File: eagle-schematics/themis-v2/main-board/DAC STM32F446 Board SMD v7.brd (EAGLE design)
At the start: 163.3 x 142.1 mm, 250 parts, among them IC1 4027D, U2 AD5328BRUZ-REEL7, U3 AD5328BRUZ-REEL7

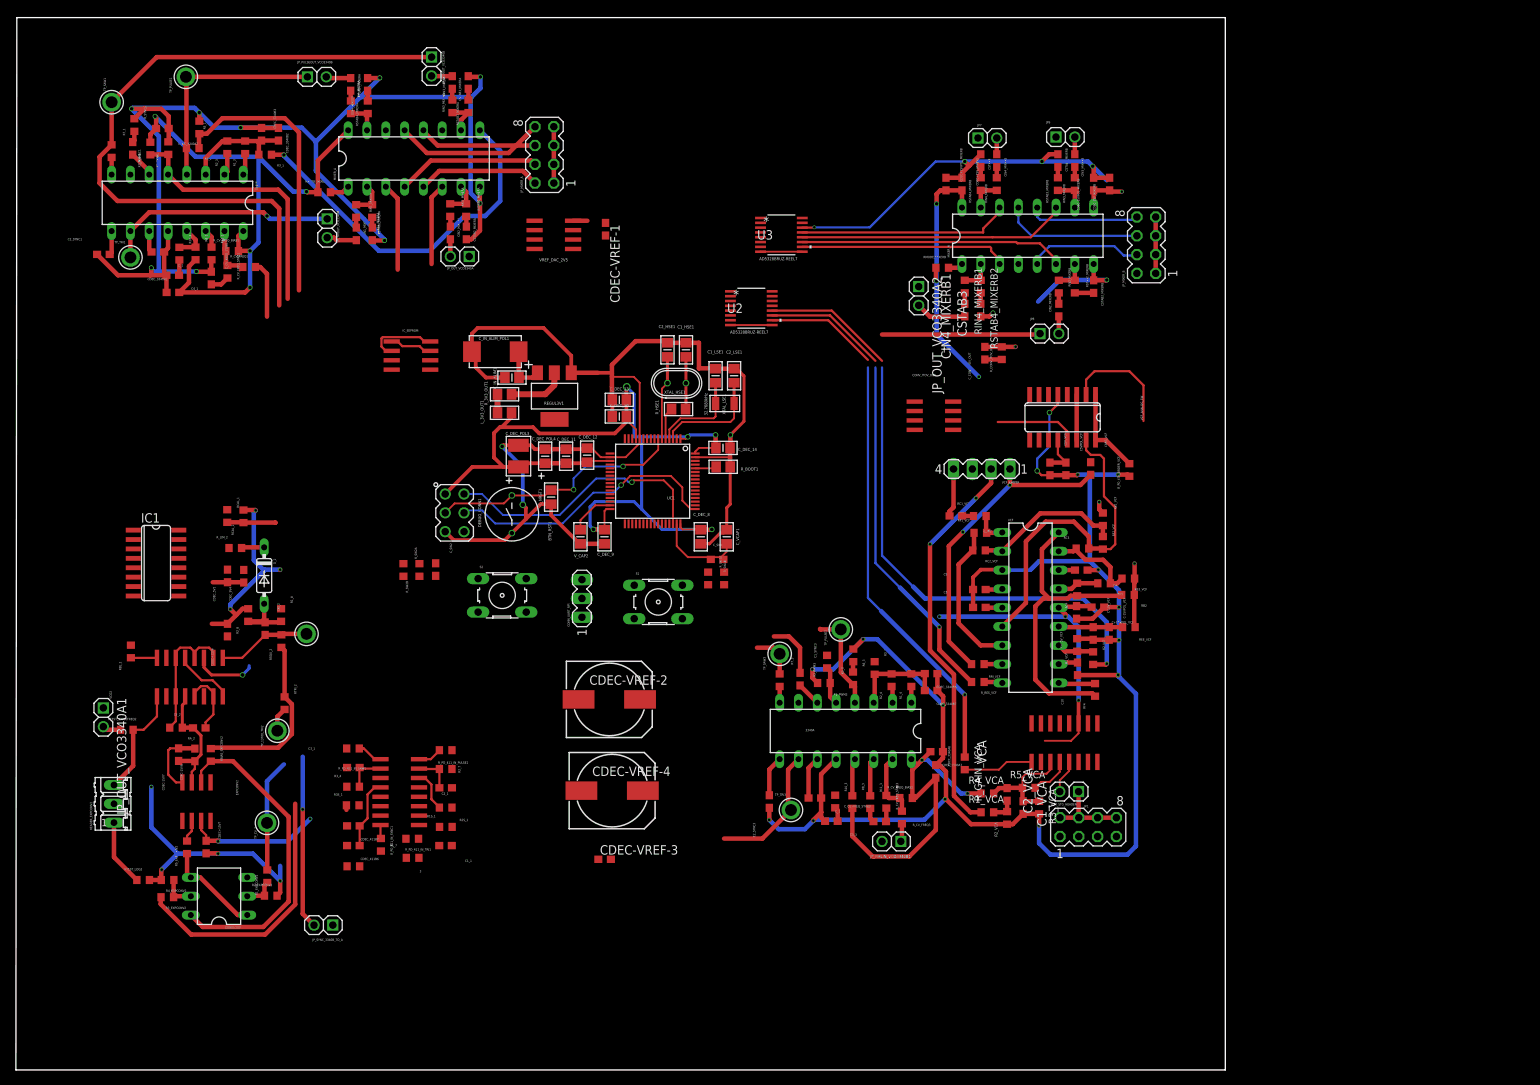
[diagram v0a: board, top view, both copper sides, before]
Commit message: started PCB routing with F446
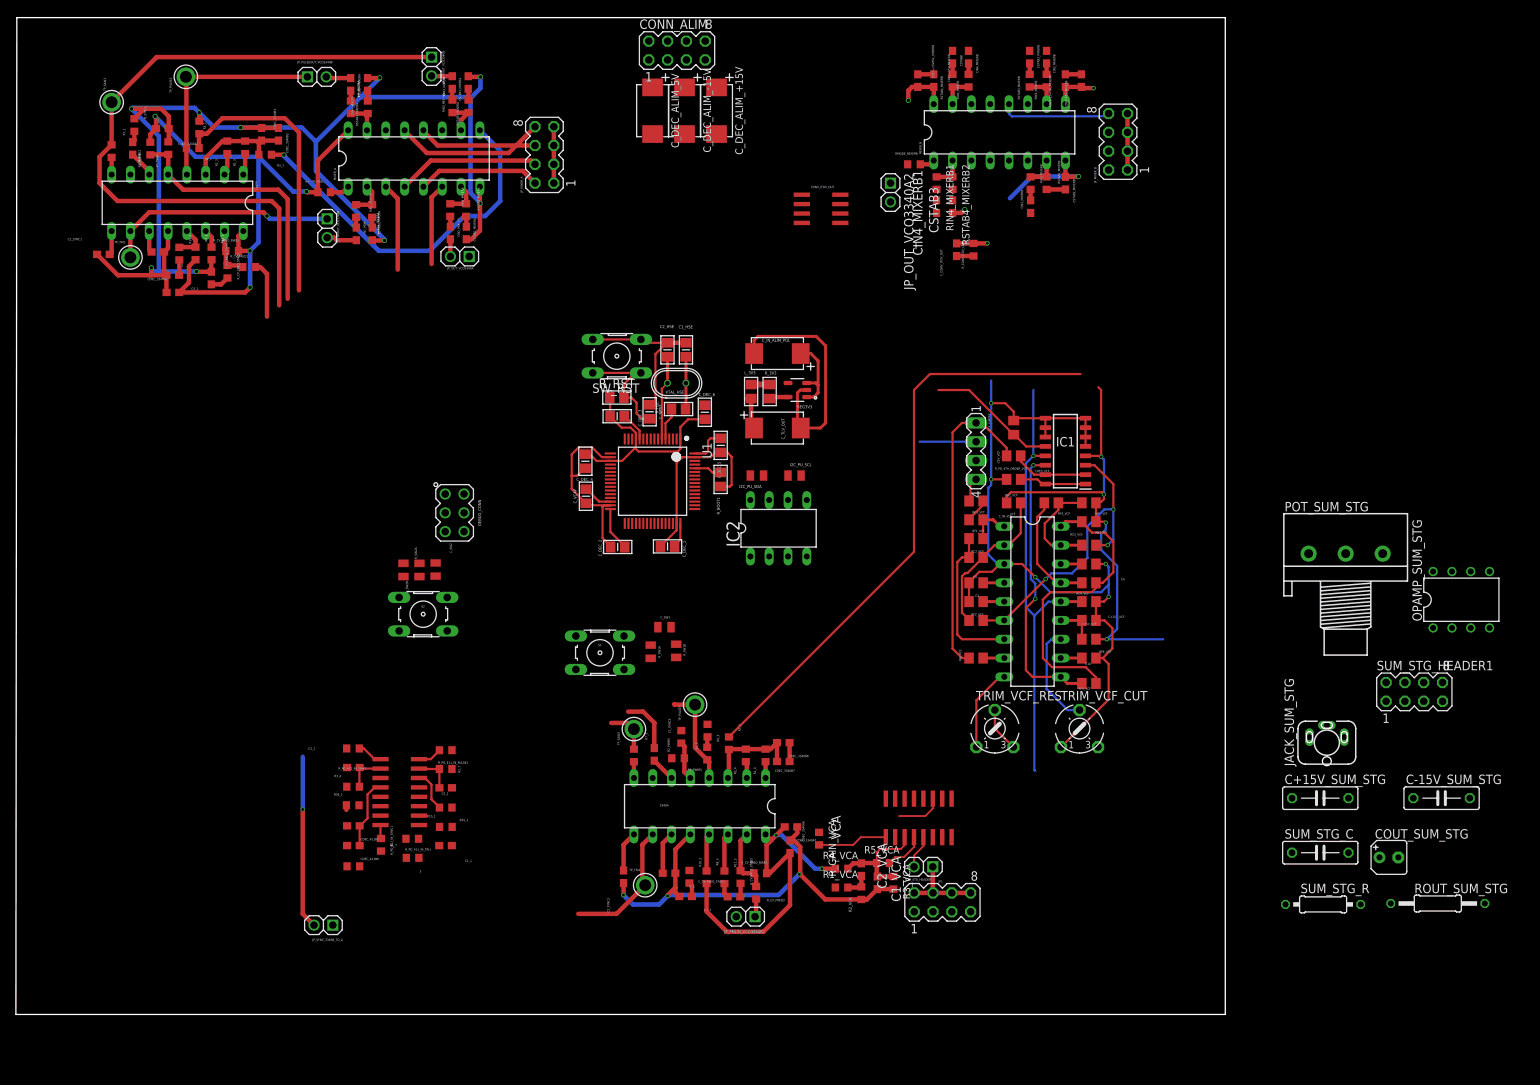
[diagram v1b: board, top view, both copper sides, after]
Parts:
- removed BTN_RST1: BUTTON-FSM14JRT, MyComponents:BUTTON-FSM14JRT
- removed C+15VPOL_VCF, C-15VPOL_VCF: 1u, rcl:C0603
- removed C1_LSE1, C2_LSE1: 22pF, MyComponents:C0805
- removed C5VPOL_VCF, CDEC+15V6, CDEC+15V7, CDEC-15V6, CDEC-15V7, CDEC-VREF-1, CDEC-VREF-3, CDEC_5V4: 100n, rcl:C0603
- removed CDEC-VREF-2: 10u, rcl:140CLH-1014
- removed CDEC-VREF-4: 100u, rcl:140CLH-1014
- removed CDEC_5V1: 10u, rcl:C0603
- removed CF_2: 100nF, rcl:C0603
- removed CIN_2, C_IN2: 470n, rcl:C0603
- removed CONN_UART_RPI: (no value), con-lstb:MA03-1
- removed CONVLOG2: BC857BS, paires_diff:DIL06
- removed C_DEC_10, C_DEC_12, C_DEC_14, C_DEC_8, C_DEC_9, C_IN_ALIM1, C_NRST1: 0.1uF, MyComponents:C0805
- removed C_DEC_11: 4.7uF, MyComponents:C0805
- removed C_DEC_13: 1.0uF, MyComponents:C0805
- removed C_DEC_POL3: 100 uF, MyComponents:CPOL1311
- removed C_DEC_POL4: 47 uF, MyComponents:CPOL0805
- removed C_IN_ALIM_POL1: 470 uF, MyComponents:CPOL2917
- removed C_VCAP1, V_CAP2: 2.2uF, MyComponents:C0805
- removed D_2: 1N4148DO35-7, diode:DO35-7
- removed EXPCONV2: TL081, linear:SO08
- removed HEADER_EXPCONV2: (no value), con-amp-quick:03P
- removed IC_EEPROM: 24C04ASN, microchip:SO-08
- removed JP7, JP8, JP9, JP_OUT_VCO3340A1: JUMPER, 6P1_EVB:HDR2X1
- removed L_3V3_OUT1: 1 uH, MyComponents:L0805
- removed R1_8, R2_8, R2_VCF, RCAL_2, RF3, RF4, R_RES_VCF: 100k, rcl:R0603
- removed R1_EXPCONV2: 330, rcl:R0603
- removed R1_VCF, RSQU_2: 10k, rcl:R0603
- removed R2_EXPCONV2, R4_EXPCONV2: 10, rcl:R0603
- removed R3_EXPCONV2: 260, rcl:R0603
- removed R5_EXPCONV2: 110, rcl:R0603
- removed RA_2: 4.7k, rcl:R0603
- removed RB2: 220k, rcl:R0603
- removed RBIAS_EXPCONV2, RCAL_1: 47k, rcl:R0603
- removed RC3, RC4: 91k, rcl:R0603
- removed REE_2, RTEST_13700FREQ2: 27k, rcl:R0603
- removed REGUL3V1: REG1117, MyComponents:SOT223
- removed RTEST_LOG2, R_LIM_2: 1k, rcl:R0603
- removed RTRI_2: 12k, rcl:R0603
- removed R_3V3_OUT1: 1, MyComponents:R0805
- removed TP_13700_SQU2, TP_13700_TRI2, TP_CV_2: (no value), 6P1_EVB:TESTPOINT_63
- removed U2, U3: AD5328BRUZ-REEL7, AD5328:RU_16
- removed UC1: STM32F405RG, stm32:LQFP64
- removed VCF_ANALOG_SW: DG413DJD, linear:SO16
- removed VCO2: LM13700M, ota:SO16
- removed VREF_DAC_2V5: AD780R, analog-devices:SO8
- removed XTAL_LSE1: 32.7680kHz, MyComponents:Q-CM7V-T1A
- added C+15V_SUM_STG, C-15V_SUM_STG: 100n, rcl:C075-032X103
- added CONN_ALIM, SUM_STG_HEADER1: (no value), con-lstb:MA04-2
- added COUT_SUM_STG: 22u, resistor:B45181A
- added C_DEC_1, C_DEC_2, C_DEC_3, C_DEC_4, C_DEC_5, C_NRST: 0.1uF, MyComponents:C0805
- added C_DEC_6: 1.0uF, MyComponents:C0805
- added C_DEC_ALIM_+15V, C_DEC_ALIM_-15V, C_DEC_ALIM_5V, C_IN_ALIM_POL: 10u, MyComponents:CPOL2917
- added C_IN_VCF: 470n, rcl:C0805
- added C_TLV_OUT: 100 uF, MyComponents:CPOL2917
- added C_VCAP: 2.2uF, MyComponents:C0805
- added I2C_PU_SCL, I2C_PU_SDA: 1k, 6P1_EVB:R0805
- added IC2: 24C04AP, microchip:DIL8
- added JACK_SUM_STG: 1502_01, con-lumberg:1502_01
- added L_3V3: 1 uH, MyComponents:L0805
- added OPAMP_SUM_STG: NE5534AN, linear:DIL08
- added POT_SUM_STG: 100kB, pot:3RP/1610N
- added RB2_VCF: 220k, rcl:R0805
- added RC3_VCF, RC4_VCF: 91k, rcl:R0805
- added REG3V3: TLV75533PDBVR, TLV75533PDBVR:SOT95P280X145-5N
- added RF3_VCF, RF4_VCF: 100k, rcl:R0805
- added ROUT_SUM_STG: 470, rcl:0207/12
- added R_3V3: 1, MyComponents:R0805
- added R_RST: 100k, MyComponents:R0805
- added SUM_STG_C: 560p, rcl:C075-032X103
- added SUM_STG_R: 27k, rcl:0207/10
- added SW_RST: (no value), switch-omron:B3F-10XX
- added TRIM_VCF_CUT, TRIM_VCF_RES: 100k, adafruit:6MM
- added U1: STM32F446RCT7, STM32F446RCT7:QFP50P1200X1200X160-64N
- C+15V_VCF, C-15V_VCF, C10, C3, C4, C5, C5V_VCF, CRES_VCF: device rcl:C0603 -> rcl:C0805
- C_SW1, C_SW2: device 6P1_EVB:C0603 -> 6P1_EVB:C0805
- IC1: value 4027D -> ADG453BRZ; device 40xx:SO16 -> ADG453BRZ:SOIC127P600X175-16N
- RB1_VCF, RB3_VCF, RC1_VCF, RC2_VCF, REE_VCF, RF1_VCF, RF2_VCF, RRI_VCF, R_PD_4TH_ORDER_VCF: device rcl:R0603 -> rcl:R0805
- R_SW1A, R_SW1B, R_SW2A, R_SW2B: device 6P1_EVB:R0603 -> 6P1_EVB:R0805
- moved IC1 123.7 mm to (141.6, 76.2), turned to 180 degrees
- moved CONV_ITOV_OUT 31.8 mm to (108.6, 108.9)
- moved JP1 22.2 mm to (123.7, 20.1)
- moved R1_4 22.2 mm to (101.1, 35.1)
- moved R1_PWM3 22.2 mm to (89.3, 34.7)
- moved R2_4 22.2 mm to (98.4, 35.1)
- moved R7_3 22.2 mm to (83.3, 35.1)
- moved 3340A 22.2 mm to (92.2, 28.2)
- moved C2_SYNC3 22.2 mm to (81.9, 18.7)
- moved C4_3 22.2 mm to (90.3, 16.1)
- moved CDEC_3340A6 22.2 mm to (104.4, 22.8)
- moved CDEC_3340A7 22.2 mm to (104.5, 25.5)
- moved C_3 22.2 mm to (88.1, 19.2)
- moved C_CV_FREQ_STAB3 22.2 mm to (96.8, 16.0)
- moved JP_FMLIN_VCO3340B1 22.2 mm to (99.7, 13.3)
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- renumbered C1_HSE1 to C1_HSE, C2_HSE1 to C2_HSE, DEBUG_CONN1 to DEBUG_CONN, R_HSE1 to R_HSE, XTAL_HSE1 to XTAL_HSE
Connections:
- removed net ALIM_CONN: C_IN_ALIM1.1, C_IN_ALIM_POL1.+, REGUL3V1.3
- removed net BIAS_4027_VCO13700: CIN_2.1, D_2.A, R1_8.2, R2_8.1
- removed net CALIB_13700: RCAL_1.2, RCAL_2.1
- removed net CV_FREQ_13700: R1_EXPCONV2.2, TP_CV_2.P$1, U2.6
- removed net DAC_LDAC: U2.1, U3.1
- removed net DAC_SYNC_CV: U2.2
- removed net DAC_SYNC_GAIN: U3.2
- removed net FM_ENTREE_13700_VCO13700: HEADER_EXPCONV2.3, RTEST_13700FREQ2.2, VCO2.1
- removed net IA_VCO13700: REE_2.1, VCO2.16
- removed net INPUT_FM_3340: JP_OUT_VCO3340A1.2, RTEST_13700FREQ2.1
- removed net N$105: C2_HSE.2, UC1.6, XTAL_HSE.2
- removed net N$106: R_HSE.1, UC1.5
- removed net N$113: CRES_VCF.1, VCF_ANALOG_SW.14, VCF_ANALOG_SW.3
- removed net N$94: EXPCONV2.6, R5_EXPCONV2.2
- removed net N$95: RA_2.2, VCO2.10, VCO2.12, VCO2.14, VCO2.3
- removed net N$96: CF_2.2, VCO2.5, VCO2.7
- removed net N$98: D_2.C, R_LIM_2.2
- removed net N$99: HEADER_EXPCONV2.1, RTEST_LOG2.1
- removed net OUT_EXPCONV_VCO13700: CONVLOG2.3, HEADER_EXPCONV2.2
- removed net PA0: UC1.14
- removed net PA1: UC1.15
- removed net PA10: UC1.43
- removed net PA15: UC1.50
- removed net PA2: UC1.16
- removed net PA3: UC1.17
- removed net PA4: UC1.20
- removed net PA5: UC1.21
- removed net PA6: UC1.22
- removed net PA7: UC1.23
- removed net PA8: UC1.41
- removed net PB0: UC1.26
- removed net PB1: UC1.27
- removed net PB10: UC1.29
- removed net PB11: UC1.30
- removed net PB12: UC1.33
- removed net PB13: UC1.34
- removed net PB14: UC1.35
- removed net PB15: UC1.36
- removed net PB2: UC1.28
- removed net PB3: UC1.55
- removed net PB4: UC1.56
- removed net PB5: UC1.57
- removed net PB6: UC1.58
- removed net PB7: UC1.59
- removed net PB8: UC1.61
- removed net PB9: UC1.62
- removed net PC0: UC1.8
- removed net PC1: UC1.9
- removed net PC10: UC1.51
- removed net PC11: UC1.52
- removed net PC12: UC1.53
- removed net PC13: UC1.2
- removed net PC2: UC1.10
- removed net PC3: UC1.11
- removed net PC4: UC1.24
- removed net PC5: UC1.25
- removed net PC6: UC1.37
- removed net PC7: UC1.38
- removed net PC8: UC1.39
- removed net PC9: UC1.40
- removed net PD2: UC1.54
- removed net PNP1_B_VCO13700: CONVLOG2.2, R1_EXPCONV2.1, R2_EXPCONV2.1
- removed net PNP1_C1_VCO1: CONVLOG2.6, EXPCONV2.2, RBIAS_EXPCONV2.2
- removed net PNP2_B_VCO13700: CONVLOG2.5, R3_EXPCONV2.1, R4_EXPCONV2.1
- removed net PNP_E1-VCO1_MIXB: CONVLOG2.1, CONVLOG2.4, R5_EXPCONV2.1
- removed net Q2M1: C2_LSE1.2, UC1.3, XTAL_LSE1.1
- removed net Q2P1: C1_LSE1.2, UC1.4, XTAL_LSE1.2
- removed net SPI_CLK: U2.16, U3.16
- removed net SPI_MOSI: U2.15, U3.15
- removed net SUBBASS_IN_VCO13700: IC1.13, R_LIM_2.1
- removed net USART_RX_RPI_TX: CONN_UART_RPI.2
- removed net USART_TX_RPI_RX: CONN_UART_RPI.3
- removed net USB-DM: UC1.44
- removed net USB-DP: UC1.45
- removed net USB-VBUS: UC1.42
- removed net VCAP2: UC1.31, V_CAP2.2
- removed net VCO13700_SQUARE: CIN_2.2, JP8.1, RSQU_2.2, TP_13700_SQU2.P$1, VCO2.9
- removed net VCO13700_SUBBASS: IC1.15, JP7.1, RCAL_1.1
- removed net VCO13700_TRI: JP9.1, RTRI_2.2, TP_13700_TRI2.P$1, VCO2.13, VCO2.8
- removed net VDD: C_DEC_10.2, C_DEC_11.2, C_DEC_12.2, C_DEC_13.2, C_DEC_14.2, C_DEC_8.2, C_DEC_9.2, C_DEC_POL3.1+, C_DEC_POL4.1+, DEBUG_CONN.1, L_3V3_OUT1.2, UC1.1, UC1.13, UC1.19, UC1.32, UC1.48, UC1.64
- removed net VREF: CDEC-VREF-4.+, U2.8, U2.9, U3.8, U3.9, VREF_DAC_2V5.6
- new net 3V3: C_DEC_1.2, C_DEC_2.2, C_DEC_3.2, C_DEC_4.2, C_DEC_5.2, C_DEC_6.2, C_TLV_OUT.+, DEBUG_CONN.1, I2C_PU_SCL.2, I2C_PU_SDA.2, IC2.2, IC2.3, IC2.8, L_3V3.2, R_RST.1, R_SW1A.1, R_SW2A.1, U1.1, U1.13, U1.19, U1.32, U1.48, U1.64
- new net CALIB_3340C: U1.16
- new net FEEDBACK_VCF: CRES_VCF.1, IC1.15, IC1.2
- new net JACK_SUM_STG: COUT_SUM_STG.-, JACK_SUM_STG.3
- new net OSC_IN: R_HSE.1, U1.5
- new net OSC_OUT: C2_HSE.2, U1.6, XTAL_HSE.2
- new net OUT_SUM_STG: OPAMP_SUM_STG.6, ROUT_SUM_STG.2, SUM_STG_C.1, SUM_STG_R.1
- new net POT2_SUM_STG: COUT_SUM_STG.+, POT_SUM_STG.2
- new net POT3_SUM_STG: POT_SUM_STG.3, ROUT_SUM_STG.1
- net +15V: now also C+15V_SUM_STG.2, CONN_ALIM.7, CONN_ALIM.8, C_DEC_ALIM_+15V.+, IC1.13, OPAMP_SUM_STG.7; no longer C+15VPOL_VCF.2, CDEC+15V6.1, CDEC+15V7.1, EXPCONV2.7, VCF_ANALOG_SW.13, VCO2.11
- net -15V: now also C-15V_SUM_STG.1, CONN_ALIM.5, CONN_ALIM.6, C_DEC_ALIM_-15V.+, IC1.4, OPAMP_SUM_STG.4, RB2_VCF.1; no longer CDEC-15V6.2, CDEC-15V7.2, EXPCONV2.4, RB2.1, RBIAS_EXPCONV2.1, RSQU_2.1, RTRI_2.1, VCF_ANALOG_SW.4, VCO2.6
- net 411_IN_PULSE: now also U1.40
- net 411_IN_SAW: now also U1.38
- net 411_IN_SYNC: now also U1.37
- net 411_IN_TRI: now also U1.39
- net 5V: now also CONN_ALIM.3, CONN_ALIM.4, C_DEC_ALIM_5V.+, C_IN_ALIM_POL.+, IC1.12, REG3V3.1, REG3V3.3; no longer C5VPOL_VCF.1, CDEC-VREF-1.2, CDEC-VREF-2.-, CDEC_5V1.1, CDEC_5V4.1, IC1.11, IC1.16, IC_EEPROM.2, IC_EEPROM.3, IC_EEPROM.8, R1_8.1, R3_EXPCONV2.2, R_SW1A.1, R_SW2A.1, U2.3, U3.3, VCF_ANALOG_SW.12, VREF_DAC_2V5.2
- net AGND: now also C+15V_SUM_STG.1, C-15V_SUM_STG.2, JACK_SUM_STG.1, OPAMP_SUM_STG.3, POT_SUM_STG.1; no longer C+15VPOL_VCF.1, C+15V_VCF.1, C-15VPOL_VCF.2, C-15V_VCF.2, C10.1, C3.1, C4.1, C5.1, C5VPOL_VCF.2, C5V_VCF.2, CDEC+15V6.2, CDEC+15V7.2, CDEC-15V6.1, CDEC-15V7.1, CDEC-VREF-1.1, CDEC-VREF-2.+, CDEC-VREF-3.2, CDEC-VREF-4.-, CDEC_5V1.2, CDEC_5V4.2, CF_2.1, CONN_UART_RPI.1, EXPCONV2.3, IC1.12, IC1.3, IC1.4, IC1.5, IC1.6, IC1.7, IC1.8, IC1.9, IC_EEPROM.1, IC_EEPROM.4, IC_EEPROM.7, R1_VCF.2, R2_8.2, R2_EXPCONV2.2, R4_EXPCONV2.2, RA_2.1, RCAL_2.2, REE_2.2, RTEST_LOG2.2, R_PD_4TH_ORDER_VCF.1, U2.14, U3.14, VCF.3, VCF_ANALOG_SW.5, VCO2.4, VREF_DAC_2V5.4, VREF_DAC_2V5.5
- net BOOT1: now also U1.60; no longer UC1.60
- net CALIB_3340A: now also U1.14
- net CALIB_3340B: now also U1.15
- net CV_CUTOFF: now also TRIM_VCF_CUT.E; no longer R2_VCF.2, U2.12
- net CV_FREQ_3340A: no longer U2.7
- net CV_FREQ_3340B: no longer U2.4
- net CV_PWM_3340A: no longer U2.13
- net CV_PWM_3340B: no longer U2.5
- net CV_RES: now also TRIM_VCF_RES.E, TRIM_VCF_RES.S; no longer R_RES_VCF.2, U2.11
- net CV_VCA: no longer U2.10
- net FREQ_CV_VCF: now also TRIM_VCF_CUT.S; no longer R1_VCF.1, R2_VCF.1
- net GAIN1_A: no longer U3.4
- net GAIN1_B: no longer U3.10
- net GAIN2_A: no longer U3.5
- net GAIN2_B: no longer U3.11
- net GAIN3_A: no longer U3.6
- net GAIN3_B: no longer U3.12
- net GAIN4_A: no longer U3.7
- net GAIN4_B: no longer U3.13
- net GND: now also C+15V_VCF.1, C-15V_VCF.2, C10.1, C3.1, C4.1, C5.1, C5V_VCF.2, CONN_ALIM.1, CONN_ALIM.2, C_DEC_1.1, C_DEC_2.1, C_DEC_3.1, C_DEC_4.1, C_DEC_5.1, C_DEC_6.1, C_DEC_ALIM_+15V.-, C_DEC_ALIM_-15V.-, C_DEC_ALIM_5V.-, C_IN_ALIM_POL.-, C_NRST.1, C_TLV_OUT.-, C_VCAP.1, IC1.10, IC1.11, IC1.5, IC1.6, IC1.7, IC1.8, IC1.9, IC2.1, IC2.4, IC2.7, REG3V3.2, R_PD_4TH_ORDER_VCF.1, SW_RST.3, SW_RST.4, TRIM_VCF_CUT.A, U1.12, U1.18, U1.31, U1.47, U1.63, VCF.3; no longer BTN_RST1.P$1, C1_LSE1.1, C2_LSE1.1, C_DEC_10.1, C_DEC_11.1, C_DEC_12.1, C_DEC_13.1, C_DEC_14.1, C_DEC_8.1, C_DEC_9.1, C_DEC_POL3.2-, C_DEC_POL4.2-, C_IN_ALIM1.2, C_IN_ALIM_POL1.-, C_NRST1.1, C_VCAP1.1, REGUL3V1.1, UC1.12, UC1.18, UC1.63, V_CAP2.1
- net IN2_MIXERA: no longer JP_OUT_VCO3340A2.1
- net IN2_MIXERB: no longer JP8.2
- net IN3_MIXERB: no longer JP9.2
- net IN3_VCF: now also RB2_VCF.2, RC3_VCF.1, RF3_VCF.1; no longer RB3_VCF.2, RC3.1, RF3.1
- net IN4_MIXERB: no longer JP7.2
- net IN4_VCF: now also RB3_VCF.2, RC4_VCF.1, RF4_VCF.1; no longer RB2.2, RC4.1, RF4.1
- net INPUT_CURRENT_SUM_STG: now also OPAMP_SUM_STG.2, SUM_STG_C.2, SUM_STG_HEADER1.1, SUM_STG_HEADER1.2, SUM_STG_HEADER1.3, SUM_STG_HEADER1.4, SUM_STG_HEADER1.5, SUM_STG_HEADER1.6, SUM_STG_HEADER1.7, SUM_STG_HEADER1.8, SUM_STG_R.2
- net IN_VCF: now also C_IN_VCF.2; no longer C_IN2.2
- net IN_VCFORDER: now also IC1.1, IC1.16; no longer VCF_ANALOG_SW.1, VCF_ANALOG_SW.16
- net N$1: now also JP_MIXER_B.2, MIXER_B.4; no longer JP_OUT_VCO3340A1.1
- net N$108: now also REG3V3.5, R_3V3.2; no longer REGUL3V1.2, R_3V3_OUT1.2
- net N$109: now also L_3V3.1, R_3V3.1; no longer L_3V3_OUT1.1, R_3V3_OUT1.1
- net N$116: now also C_IN_VCF.1; no longer C_IN2.1
- net N$3: now also JP_OUT_VCO3340A2.1; no longer CDEC-VREF-3.1, VREF_DAC_2V5.3
- net N$6: now also U1.10, U1.20, U1.21, U1.23, U1.29, U1.33, U1.34, U1.35, U1.36, U1.50, U1.51, U1.58, U1.59, U1.9; no longer IC1.10, IC1.14
- net NRST: now also C_NRST.2, R_RST.2, SW_RST.1, SW_RST.2, U1.7; no longer BTN_RST1.P$2, C_NRST1.2, UC1.7
- net OUT2_VCF: now also IC1.3, RC3_VCF.2; no longer RC3.2, VCF_ANALOG_SW.15
- net OUT3_VCF: now also RC4_VCF.2, RF3_VCF.2; no longer RC4.2, RF3.2
- net OUT4_VCF: now also IC1.14, RF4_VCF.2; no longer RF4.2, VCF_ANALOG_SW.2
- net RES_CUR_VCF: now also TRIM_VCF_RES.A; no longer R_RES_VCF.1
- net SCL: now also I2C_PU_SCL.1, IC2.6, U1.61; no longer IC_EEPROM.6
- net SDA: now also I2C_PU_SDA.1, IC2.5, U1.62; no longer IC_EEPROM.5
- net SWCLK: now also U1.49; no longer UC1.49
- net SWDIO: now also U1.46; no longer UC1.46
- net VCAP1: now also C_VCAP.2, U1.30; no longer C_VCAP1.2, UC1.47
- net VEE_VCF: no longer C-15VPOL_VCF.1
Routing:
- net AGND: track 574.3 -> 259.9 mm, vias 37 -> 14
- net VDD: track 126.3 -> 0.00 mm, vias 5 -> 0
- net -15V: track 99.3 -> 200.4 mm, vias 4 -> 6
- net CV_CUTOFF: track 84.6 -> 0.00 mm, vias 1 -> 0
- net CV_VCA: track 73.2 -> 0.00 mm, vias 1 -> 0
- net CV_RES: track 64.3 -> 6.04 mm, vias 1 -> 0
- net GND: track 164.8 -> 219.1 mm, vias 3 -> 5
- net 3V3: track 0.00 -> 49.3 mm
- net IN_VCA: track 53.5 -> 7.62 mm, vias 2 -> 0
- net PNP1_C1_VCO1: track 43.8 -> 0.00 mm
- net +15V: track 242.7 -> 200.4 mm, vias 15 -> 8
- net SWCLK: track 37.7 -> 0.00 mm, vias 1 -> 0
- net SWDIO: track 36.9 -> 0.00 mm, vias 1 -> 0
- net GAIN3_B: track 36.3 -> 0.00 mm
- net GAIN2_B: track 35.8 -> 0.00 mm
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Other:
- board size 163.3 x 142.1 mm -> 163.3 x 134.6 mm

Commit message: PCB for F446
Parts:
- removed 3: ADG411R, analog-devices:SOIC16N
- removed C+15V_SUM_STG, C-15V_SUM_STG: 100n, rcl:C075-032X103
- removed C+15V_VCF, C-15V_VCF, C5V_VCF: 100n, rcl:C0805
- removed C1_1, C2_1, C3_1, CIN1_MIXERA, CIN2_MIXERA, CIN2_MIXERB, CIN3_MIXERA, CIN3_MIXERB, CIN4_MIXERA, CIN4_MIXERB, CIN4_MIXERB1: 470n, rcl:C0603
- removed C1_HSE, C2_HSE: 12pF, MyComponents:C0805
- removed C1_SYNC1, C1_SYNC3, C_1, C_3: 1n, rcl:C0603
- removed C1_VCA, C2_VCA: 4.7u, rcl:C0603
- removed C2_SYNC1, C2_SYNC3, CDEC+15VPOL_MIXERB, CDEC+15V_MIXERB, CDEC-15VPOL_MIXERB, CDEC-15V_MIXERB, CDEC_3340A2, CDEC_3340A6, CDEC_3340B2, CDEC_3340B6, CDEC_411B6: 100n, rcl:C0603
- removed C4_1, C4_3, C_CV_FREQ_STAB1, C_CV_FREQ_STAB3: 10n, rcl:C0603
- removed CDEC_3340A3, CDEC_3340A7, CDEC_3340B3, CDEC_3340B7, CDEC_411B7: 10u, rcl:C0603
- removed CONN_ALIM, JP_MIXER_A, JP_MIXER_B, SUM_STG_HEADER, SUM_STG_HEADER1: (no value), con-lstb:MA04-2
- removed CONV_ITOV_OUT: NE5534AD, linear:SO08
- removed COUT_SUM_STG: 22u, resistor:B45181A
- removed CRES_VCF: 1u, rcl:C0805
- removed CSTAB1_MIXERA, CSTAB2_MIXERA, CSTAB2_MIXERB, CSTAB3, CSTAB3_MIXERA, CSTAB3_MIXERB, CSTAB4_MIXERA, CSTAB8: 560p, rcl:C0603
- removed C_CONV_ITOV_OUT: 1p, rcl:C0603
- removed C_DEC_1, C_DEC_2, C_DEC_3, C_DEC_4, C_DEC_5, C_NRST: 0.1uF, MyComponents:C0805
- removed C_DEC_6: 1.0uF, MyComponents:C0805
- removed C_DEC_ALIM_+15V, C_DEC_ALIM_-15V, C_DEC_ALIM_5V, C_IN_ALIM_POL: 10u, MyComponents:CPOL2917
- removed C_IN_VCF: 470n, rcl:C0805
- removed C_SW1, C_SW2: 100n, 6P1_EVB:C0805
- removed C_TLV_OUT: 100 uF, MyComponents:CPOL2917
- removed C_VCAP: 2.2uF, MyComponents:C0805
- removed DEBUG_CONN: 75867-331LF, MyComponents:MA03-2
- removed I2C_PU_SCL, I2C_PU_SDA: 1k, 6P1_EVB:R0805
- removed IC1: ADG453BRZ, ADG453BRZ:SOIC127P600X175-16N
- removed IC2: 24C04AP, microchip:DIL8
- removed JACK_SUM_STG: 1502_01, con-lumberg:1502_01
- removed JP1, JP_FMLIN_VCO3340B1, JP_OUT_VCO3340A, JP_OUT_VCO3340A2, JP_PULSEOUT_VCO3340B, JP_SAWOUT_VCO3340B, JP_SYNC_3340B_TO_A, JP_TRIOUT_VCO3340B: JUMPER, 6P1_EVB:HDR2X1
- removed L_3V3: 1 uH, MyComponents:L0805
- removed MIXER_A, MIXER_B: SSM2164_MULTI, analog-audio-chips:DIL16
- removed OPAMP_SUM_STG: NE5534AN, linear:DIL08
- removed POT_SUM_STG: 100kB, pot:3RP/1610N
- removed R10_1, R10_3, RSTAB1_MIXERA, RSTAB2_MIXERA, RSTAB2_MIXERB, RSTAB3_MIXERA, RSTAB3_MIXERB, RSTAB4_MIXERA, RSTAB4_MIXERB, RSTAB4_MIXERB2, R_CV_FREQ_STAB1, R_CV_FREQ_STAB3: 470, rcl:R0603
- removed R11_1, R11_3: 1.8k, rcl:R0603
- removed R1S_1, R2S_1, R3S_1: 1k, rcl:R0603
- removed R1_3, R1_4: 30k, rcl:R0603
- removed R1_7, R2_7, R3_4, R5_VCA, R_PD_411_IN_PULSE1, R_PD_411_IN_SAW1, R_PD_411_IN_SYNC1, R_PD_411_IN_TRI1: 100k, rcl:R0603
- removed R1_PWM1, R1_PWM3, R_CV_FREQ1, R_CV_FREQ3: 68k, rcl:R0603
- removed R1_VCA, R2_VCA, R3_VCA, R4_VCA, R5_1, R5_3: 10k, rcl:R0603
- removed R2_3, R2_4, R7_1, R7_3: 5.6k, rcl:R0603
- removed R2_PWM1, R2_PWM3: 330k, rcl:R0603
- removed R3_1, R3_3: 820, rcl:R0603
- removed R6_1, R6_3: 33k, rcl:R0603
- removed R8_1, R8_3: 1.5M, rcl:R0603
- removed RB1_VCF, RB2_VCF, RB3_VCF: 220k, rcl:R0805
- removed RC1_VCF, RC2_VCF, RC3_VCF, RC4_VCF: 91k, rcl:R0805
- removed REE_VCF: 1.5k, rcl:R0805
- removed REG3V3: TLV75533PDBVR, TLV75533PDBVR:SOT95P280X145-5N
- removed RF1_VCF, RF2_VCF, RF3_VCF, RF4_VCF, R_PD_4TH_ORDER_VCF: 100k, rcl:R0805
- removed RIN1_MIXERA, RIN2_MIXERA, RIN2_MIXERB, RIN3_MIXERA, RIN3_MIXERB, RIN4_MIXERA, RIN4_MIXERB, RIN4_MIXERB1: 27k, rcl:R0603
- removed RMODE_MIXERA, RMODE_MIXERB: 8.2k, rcl:R0603
- removed ROUT_SUM_STG: 470, rcl:0207/12
- removed RRI_VCF: 51k, rcl:R0805
- removed R_3V3: 1, MyComponents:R0805
- removed R_BOOT1: 10K, MyComponents:R0805
- removed R_CONV_ITOV_OUT: 33K, rcl:R0603
- removed R_CV_FREQ_BIAS1, R_CV_FREQ_BIAS3: 270k, rcl:R0603
- removed R_GAIN_VCA: 47k, rcl:R0603
- removed R_HSE: 100, MyComponents:R0805
- removed R_RST: 100k, MyComponents:R0805
- removed R_SW1A, R_SW1B, R_SW2A, R_SW2B: 10k, 6P1_EVB:R0805
- removed R_SYNC1, R_SYNC3: 470k, rcl:R0603
- removed S1, S2, SW_RST: (no value), switch-omron:B3F-10XX
- removed SUM_STG_C: 560p, rcl:C075-032X103
- removed SUM_STG_R: 27k, rcl:0207/10
- removed TP_PULSE1, TP_PULSE3, TP_SAW1, TP_SAW3, TP_TRI1, TP_TRI3: (no value), 6P1_EVB:TESTPOINT_63
- removed TRIM_VCF_CUT, TRIM_VCF_RES: 100k, adafruit:6MM
- removed U1: STM32F446RCT7, STM32F446RCT7:QFP50P1200X1200X160-64N
- removed VCF: AS3320, analog-audio-chips:DIL18
- removed VCF_JUMPER: (no value), con-lstb:MA04-1
- removed XTAL_HSE: 16MHz, MyComponents:Q-HC-46X
- added 0V/5V/-15V/+15V, SUM_CON: (no value), con-lstb:MA04-2
- added 2164A, 2164B: SSM2164, analog-audio-chips:DIL16
- added 24C04: 24C04AP, microchip:DIL8
- added A010/9/8/7/3/4/5/6: (no value), con-lstb:MA08-1
- added A02/1/12/11, ABCD: (no value), con-lstb:MA04-1
- added A1, A2, A3, A4, B1, B2, B3, B4, SUB2, SUB4, SUB_IN, TRI_A, TRI_B: T, 6P1_EVB:TESTPOINT_63
- added AD5644: ANALOG_DEVICES_AD5644RBRMZ-5ANALOG_DEVICES_AD5644RBRMZ-5_0_0, Analog Devices - AD5644RBRMZ-5:ANALOG_DEVICES_AD5644RBRMZ-5_0
- added ADG453: ADG453BRZ, ADG453BRZ:SOIC127P600X175-16N
- added BH2221: BH2221FV, BH2221FV:SOP65P780X200-20N
- added C1, C11, C16, C2, C33, C34, C39, C40, C51, C6, C9: 100n, rcl:C0805
- added C12, C13, C14, C15: 10n, rcl:C0805
- added C17, C18, C19, C20, C21, C22, C23, C24, C41: 470n, rcl:C0805
- added C25, C26, C27, C28, C29, C30, C31, C32: 560p, rcl:C0805
- added C35: 1p, rcl:C0805
- added C36, C37, C38: 4.7u, rcl:C0805
- added C42, C44: 1u, rcl:C0805
- added C43, C45, C49, C52: 300p, rcl:C0805
- added C46: 100p, rcl:C0805
- added C47, C48, C61, C72: 100n, rcl:C1206
- added C50: 22u, resistor:B45181A
- added C53, C54, C58, C59, C62, C73: 10u, MyComponents:CPOL2917
- added C55, C66, C67, C68, C69, C70: 0.1uF, MyComponents:C0805
- added C56, C57: 12pF, MyComponents:C0805
- added C60: 2.2uF, MyComponents:C0805
- added C63, C64: 100n, 6P1_EVB:C0805
- added C65: 100 uF, MyComponents:CPOL2917
- added C7, C8: 1n, rcl:C0805
- added C71: 1.0uF, MyComponents:C0805
- added CAL_A, SYNC_A, SYNC_B: SYNC_IN, 6P1_EVB:TESTPOINT_63
- added CAL_B: CALIB B, 6P1_EVB:TESTPOINT_63
- added CAL_IN_A, CAL_IN_B, CUTOFF, IN10, IN9, MIXOUT, Q, VCA_CV, VCA_IN, VCA_OUT, VCF_IN, VCF_OUT, XIN, XMOD: (no value), 6P1_EVB:TESTPOINT_63
- added CV_A, CV_B: CV, 6P1_EVB:TESTPOINT_63
- added CV_TM, HIGH_A, HIGH_B, LOW_A, LOW_B, Q_TM: 100k, adafruit:6MM
- added F446: STM32F446RCT7, STM32F446RCT7:QFP50P1200X1200X160-64N
- added FM_B: FMLIN, 6P1_EVB:TESTPOINT_63
- added GAINS: GAIN_CTRL, con-lstb:MA08-1
- added IN34: IN34, stm32_pi_board:MA02-1
- added ITOV, SUM_OPAMP: NE5534AN, linear:DIL08
- added I_SUM: ITOV, con-lstb:MA08-2
- added JACK: 1502_01, con-lumberg:1502_01
- added L1: 1 uH, MyComponents:L0805
- added MODRING: LM13700M, ota:SO16
- added Q1: 16MHz, MyComponents:Q-HC-46X
- added R1, R3: 330k, rcl:R0805
- added R10, R9: 820, rcl:R0805
- added R11, R12: 24k, rcl:R0805
- added R13, R27: 470k, rcl:R0805
- added R14, R15, R16, R17: 5.6k, rcl:R0805
- added R18, R19: 1.8k, rcl:R0805
- added R2, R4: 68k, rcl:R0805
- added R20, R22, R23, R24, R32, R37, R38, R39, R40, R41, R42, R43, R73: 470, rcl:R0805
- added R21: 1M, rcl:R0805
- added R25, R26: 1.5M, rcl:R0805
- added R28, R29, R30, R31, R33, R34, R35, R36, R46, R47, R58: 27k, rcl:R0805
- added R44, R45: 8.2k, rcl:R0805
- added R48: 33K, rcl:R0805
- added R49, R53, R62, R66, R67, R68, R72, R74, R78: 100k, rcl:R0805
- added R5, R51, R52, R6, R63: 10k, rcl:R0805
- added R50, R56: 1k, rcl:R0805
- added R54: 1.5k, rcl:R0805
- added R55: 51k, rcl:R0805
- added R57: 4.7k, rcl:R0805
- added R59, R64, R70, R76: 91k, rcl:R0805
- added R60, R69: 47k, rcl:R0805
- added R61: 22k, rcl:R0805
- added R65, R71, R77: 220k, rcl:R0805
- added R7, R8: 33k, rcl:R0805
- added R75: 100kB, pot:3RP/1610N
- added R79: 100k, MyComponents:R0805
- added R80: 100, MyComponents:R0805
- added R81: 10K, MyComponents:R0805
- added R82, R83, R85, R86: 10k, 6P1_EVB:R0805
- added R84, R88: 1k, 6P1_EVB:R0805
- added R87: 1, MyComponents:R0805
- added RST, SW1, SW2: (no value), switch-omron:B3F-10XX
- added SAW_A, SAW_B: S, 6P1_EVB:TESTPOINT_63
- added SD3: SD3, stm32_pi_board:MA02-1
- added SD4: SD4, stm32_pi_board:MA02-1
- added SQU_A, SQU_B: P, 6P1_EVB:TESTPOINT_63
- added STLINK: 75867-331LF, MyComponents:MA03-2
- added SUB: 4027D, 40xx:SO16
- added TEMCOA, TEMCOB: 10k, adafruit:6MM
- added TLV75533: TLV75533PDBVR, TLV75533PDBVR:SOT95P280X145-5N
- added VCF1: AS3320, analog-audio-chips:DIL18
- C10, C5: value 300p -> 100n
- C3, C4: value 300p -> 1n
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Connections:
- removed net 2164_MODE_MIXA: MIXER_A.1, RMODE_MIXERA.2
- removed net 411_IN_PULSE: 3.8, R_PD_411_IN_PULSE1.2, U1.40
- removed net 411_IN_SAW: 3.9, R_PD_411_IN_SAW1.1, U1.38
- removed net 411_IN_SYNC: 3.16, R_PD_411_IN_SYNC1.1, U1.37
- removed net 411_IN_TRI: 3.1, R_PD_411_IN_TRI1.1, U1.39
- removed net AGND: 3.5, 3340A.12, 3340B.12, C+15V_SUM_STG.1, C-15V_SUM_STG.2, C1_VCA.2, C2_SYNC1.1, C2_SYNC3.1, C4_1.2, C4_3.2, CDEC+15VPOL_MIXERB.1, CDEC+15V_MIXERB.1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
- removed net CALIB_3340C: U1.16
- removed net FREQ_CTRL_VCOA: 3340A.15, R_CV_FREQ3.1, R_CV_FREQ_BIAS3.1, R_CV_FREQ_STAB3.1
- removed net FREQ_CTRL_VCOB: 3340B.15, R_CV_FREQ1.1, R_CV_FREQ_BIAS1.1, R_CV_FREQ_STAB1.1
- removed net HARD_SYNC_VCOA: 3340A.6, C1_SYNC3.2
- removed net HARD_SYNC_VCOB: 3340B.6, C1_SYNC1.2
- removed net IN4_MIXERA: CIN4_MIXERA.1, JP_PULSEOUT_VCO3340B.2
- removed net INPUT_CURRENT_SUM_STG: JP1.1, JP1.2, OPAMP_SUM_STG.2, SUM_STG_C.2, SUM_STG_HEADER.2, SUM_STG_HEADER.4, SUM_STG_HEADER.6, SUM_STG_HEADER.8, SUM_STG_HEADER1.1, SUM_STG_HEADER1.2, SUM_STG_HEADER1.3, SUM_STG_HEADER1.4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
- removed net IN_VCA: R1_VCA.1, VCF_JUMPER.2
- removed net JACK_SUM_STG: COUT_SUM_STG.-, JACK_SUM_STG.3
- removed net LINEAR_CTRL_VCOA: 3340A.13, R10_3.1, R8_3.1
- removed net LINEAR_CTRL_VCOB: 3340B.13, R10_1.1, R8_1.1
- removed net MIXER_OUT1: CONV_ITOV_OUT.2, C_CONV_ITOV_OUT.1, JP_MIXER_A.1, JP_MIXER_A.3, JP_MIXER_A.5, JP_MIXER_A.7, JP_MIXER_B.1, JP_MIXER_B.3, JP_MIXER_B.5, JP_MIXER_B.7, R_CONV_ITOV_OUT.1
- removed net N$82: C_CV_FREQ_STAB1.2, R_CV_FREQ_STAB1.2
- removed net N$83: C4_1.1, R10_1.2
- removed net N$86: C_CV_FREQ_STAB3.2, R_CV_FREQ_STAB3.2
- removed net N$87: C4_3.1, R10_3.2
- removed net N$88: 3.2, C1_1.2, R1_7.2
- removed net N$89: 3.7, C2_1.2, R2_7.2
- removed net N$90: 3.10, C3_1.2, R3_4.2
- removed net N$91: 3.6, R2S_1.2
- removed net OUT_SUM_STG: OPAMP_SUM_STG.6, ROUT_SUM_STG.2, SUM_STG_C.1, SUM_STG_R.1
- removed net POT2_SUM_STG: COUT_SUM_STG.+, POT_SUM_STG.2
- removed net POT3_SUM_STG: POT_SUM_STG.3, ROUT_SUM_STG.1
- removed net PULSE_OUT_VCOA: 3.11, R3S_1.2
- removed net PULSE_VCOA: 3340A.4, C3_1.1, R6_3.2, TP_PULSE3.P$1
- removed net SAW_3340_VCOA: C2_1.1, R7_3.1, TP_SAW3.P$1
- removed net SAW_VCOA: 3340A.8, R7_3.2
- removed net SAW_VCOB: 3340B.8, R7_1.2
- removed net SCALE_VCOA: 3340A.14, R11_3.1
- removed net SCALE_VCOB: 3340B.14, R11_1.1
- removed net SOFT_SYNC_VCOA: 3340A.9, C2_SYNC3.2
- removed net SOFT_SYNC_VCOB: 3340B.9, C2_SYNC1.2
- removed net SYNC_3340_VCOA: 3.15, C1_SYNC3.1, R_SYNC3.2
- removed net SYNC_3340_VCOB: C1_SYNC1.1, R_SYNC1.2
- removed net SYNC_IN_VCOA: 3.14, JP_SYNC_3340B_TO_A.1
- removed net TEMPCO1_VCOA: 3340A.1, R1_4.1
- removed net TEMPCO1_VCOB: 3340B.1, R1_3.1
- removed net TIMING_CAP_VCOA: 3340A.11, C_3.2
- removed net TIMING_CAP_VCOB: 3340B.11, C_1.2
- removed net TRI_3340_VCOA: 3340A.10, C1_1.1, TP_TRI3.P$1
- removed net TRI_OUT_VCOA: 3.3, R1S_1.1
- removed net VCO3340B_PULSE_OUT: 3340B.4, JP_PULSEOUT_VCO3340B.1, R6_1.2, TP_PULSE1.P$1
- removed net VCO3340B_SAW_OUT: JP_SAWOUT_VCO3340B.1, JP_SYNC_3340B_TO_A.2, R7_1.1, TP_SAW1.P$1
- removed net VCO3340B_TRI_OUT: 3340B.10, JP_TRIOUT_VCO3340B.1, TP_TRI1.P$1
- removed net VCO440A_OUT: JP_OUT_VCO3340A.1, R1S_1.2, R2S_1.1, R3S_1.1
- new net AD5644_CLK: AD5644.7, F446.29
- new net AD5644_DI: AD5644.8, F446.9
- new net AD5644_SYNC: AD5644.6, F446.33
- new net BH2221_CLK: BH2221.16, F446.21
- new net BH2221_DI: BH2221.17, F446.23
- new net BH2221_LD: BH2221.15, F446.20
- new net CALIB_IN_3340A: CAL_IN_A.P$1, F446.14
- new net CALIB_IN_3340B: CAL_IN_B.P$1, F446.15
- new net FMLIN_3340B: C11.2, FM_B.P$1
- new net FREQ_CTRL_3340A: 3340A.15, HIGH_A.A, HIGH_A.S, LOW_A.A, LOW_A.S, R24.1
- new net FREQ_CTRL_3340B: 3340B.15, HIGH_B.A, HIGH_B.S, LOW_B.A, LOW_B.S, R23.1
- new net HEADIN_OPAMP_OUT: C46.2, R69.2, SUM_CON.1, SUM_CON.2, SUM_CON.3, SUM_CON.4, SUM_CON.5, SUM_CON.6, SUM_CON.7, SUM_CON.8, SUM_OPAMP.2
- new net IOUT_VCA: VCA.5, VCA_OUT.P$1
- new net ITOV_IN: C35.1, ITOV.2, I_SUM.1, I_SUM.11, I_SUM.13, I_SUM.15, I_SUM.3, I_SUM.5, I_SUM.7, I_SUM.9, R46.1, R47.1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
- new net LINEAR_CTRL_3340A: 3340A.13, R22.1, R26.1
- new net LINEAR_CTRL_3340B: 3340B.13, R20.1, R21.1, R25.1
- new net N$14: IN9.P$1, R46.2
- new net N$15: IN10.P$1, R47.2
- new net N$16: ADG453.7, SD4.1
- new net N$171: C12.2, R23.2
- new net N$172: C14.1, R20.2
- new net N$173: 3340B.1, TEMCOB.A
- new net N$174: R11.1, TEMCOB.E, TEMCOB.S
- new net N$175: C11.1, R21.2
- new net N$176: 3340B.8, R14.2
- new net N$18: ADG453.11, SD3.1
- new net N$19: A010/9/8/7/3/4/5/6.5, BH2221.2
- new net N$21: A010/9/8/7/3/4/5/6.6, BH2221.3
- new net N$23: A010/9/8/7/3/4/5/6.7, BH2221.4
- new net N$25: A010/9/8/7/3/4/5/6.8, BH2221.5
- new net N$26: A010/9/8/7/3/4/5/6.4, BH2221.6
- new net N$27: A010/9/8/7/3/4/5/6.3, BH2221.7
- new net N$28: A010/9/8/7/3/4/5/6.2, BH2221.8
- new net N$29: A010/9/8/7/3/4/5/6.1, BH2221.9
- new net N$30: A02/1/12/11.1, BH2221.19
- new net N$301: C13.2, R24.2
- new net N$302: C15.1, R22.2
- new net N$303: 3340A.1, TEMCOA.A
- new net N$304: R12.1, TEMCOA.E, TEMCOA.S
- new net N$306: 3340A.8, R15.2
- new net N$307: 3340A.6, C4.2
- new net N$31: A02/1/12/11.2, BH2221.18
- new net N$32: A02/1/12/11.3, BH2221.13
- new net N$33: A02/1/12/11.4, BH2221.12
- new net N$34: ABCD.1, AD5644.1
- new net N$35: ABCD.2, AD5644.2
- new net N$36: ADG453.10, SD3.2
- new net N$37: ADG453.9, IN34.1, R72.1
- new net N$38: 2164A.1, R45.2
- new net N$39: ABCD.3, AD5644.4
- new net N$40: ABCD.4, AD5644.5
- new net N$41: SUB.2, SUB.6
- new net N$42: C16.1, SUB.11, SUB.16, SUB.5
- new net N$43: C38.1, R53.1
- new net N$44: MODRING.9, R63.2
- new net N$45: C42.1, MODRING.16, R60.1
- new net N$46: C42.2, R57.1
- new net N$47: C36.1, R50.1, VCA.3
- new net N$49: R57.2, XMOD.P$1
- new net N$50: C38.2, XIN.P$1
- new net N$51: MODRING.10, MODRING.12, R61.2
- new net N$8: C3.1, R13.2, SYNC_B.P$1
- new net N$9: ADG453.6, SD4.2
- new net OUT_JACK: C50.-, JACK.2, JACK.3
- new net OUT_OPAMP: C46.1, R69.1, R73.2, SUM_OPAMP.6
- new net OUT_POT: C50.+, R73.1, R75.2, R75.3
- new net PULSE_3340A: 3340A.4, R8.2, SQU_A.P$1
- new net PULSE_3340B: 3340B.4, R7.2, SQU_B.P$1
- new net SAW_3340A: R15.1, SAW_A.P$1
- new net SAW_3340B: R14.1, SAW_B.P$1
- new net SCALE_3340A: 3340A.14, R19.1
- new net SCALE_3340B: 3340B.14, R18.1
- new net SOFT_SYNC_3340A: 3340A.9, C10.2
- new net SOFT_SYNC_3340B: 3340B.9, C9.2
- new net SUB_IN: SUB.3, SUB_IN.P$1
- new net SUB_OUT2: SUB.1, SUB.13, SUB2.P$1
- new net SUB_OUT4: SUB.15, SUB4.P$1
- new net SYNC_3340A: C4.1, R27.2, SYNC_A.P$1
- new net TIMING_CAP_3340A: 3340A.11, C8.2
- new net TIMING_CAP_3340B: 3340B.11, C7.2
- new net TRI_3340A: 3340A.10, TRI_A.P$1
- new net TRI_3340B: 3340B.10, TRI_B.P$1
- new net VCA_IN: R49.1, VCA_IN.P$1
- new net VCF_ANASW_IN4: ADG453.8, IN34.2, R66.2
- new net VSS: SUB.8
- net +15V: now also 0V/5V/-15V/+15V.7, 0V/5V/-15V/+15V.8, 2164A.16, 2164B.16, ADG453.13, C33.2, C39.2, C47.2, C5.2, C53.+, C6.2, ITOV.7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; no longer 3.13, C+15V_SUM_STG.2, C+15V_VCF.2, CDEC+15VPOL_MIXERB.2, CDEC+15V_MIXERB.2, CDEC_3340A2.2, CDEC_3340A3.2, CDEC_3340A6.2, CDEC_3340A7.2, CONN_ALIM.7, CONN_ALIM.8, CONV_ITOV_OUT.7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
- net -15V: now also 0V/5V/-15V/+15V.5, 0V/5V/-15V/+15V.6, 2164A.9, 2164B.9, ADG453.4, C34.1, C48.1, C54.+, ITOV.4, MODRING.6, R10.1, R54.1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; no longer 3.4, C-15V_SUM_STG.1, CDEC-15VPOL_MIXERB.1, CDEC-15V_MIXERB.1, CONN_ALIM.5, CONN_ALIM.6, CONV_ITOV_OUT.4, C_DEC_ALIM_-15V.+, IC1.4, MIXER_A.9, MIXER_B.9, OPAMP_SUM_STG.4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
- net 2164_IN1_MIXA: now also 2164A.2, R33.1, R40.1; no longer MIXER_A.2, RIN1_MIXERA.1, RSTAB1_MIXERA.1
- net 2164_IN2_MIXA: now also 2164A.7, R34.1, R41.1; no longer MIXER_A.7, RIN2_MIXERA.1, RSTAB2_MIXERA.1
- net 2164_IN2_MIXB: now also 2164B.7, R29.1, R37.1; no longer MIXER_B.7, RIN2_MIXERB.1, RSTAB2_MIXERB.1
- net 2164_IN3_MIXA: now also 2164A.10, R35.1, R42.1; no longer MIXER_A.10, RIN3_MIXERA.1, RSTAB3_MIXERA.1
- net 2164_IN3_MIXB: now also 2164B.10, R30.1, R38.1; no longer MIXER_B.10, RIN3_MIXERB.1, RSTAB3_MIXERB.1
- net 2164_IN4_MIXA: now also 2164A.15, R36.1, R43.1; no longer MIXER_A.15, RIN4_MIXERA.1, RSTAB4_MIXERA.1
- net 2164_IN4_MIXB: now also 2164B.15, R31.1, R39.1; no longer MIXER_B.15, RIN4_MIXERB.1, RSTAB4_MIXERB.1
- net 2164_IN4_MIXB1: now also 2164B.2, R28.1, R32.1; no longer MIXER_B.2, RIN4_MIXERB1.1, RSTAB4_MIXERB2.1
- net 2164_MODE_MIXB: now also 2164B.1, R44.2; no longer MIXER_B.1, RMODE_MIXERB.2
- net 2164_OUT2_MIXA: now also 2164A.5, I_SUM.4; no longer JP_MIXER_A.2, MIXER_A.5
- net 2164_OUT2_MIXB: now also 2164B.5, I_SUM.14; no longer JP_MIXER_B.4, MIXER_B.5
- net 2164_OUT3_MIXA: now also 2164A.12, I_SUM.8; no longer JP_MIXER_A.6, MIXER_A.12
- net 2164_OUT3_MIXB: now also 2164B.12, I_SUM.16; no longer JP_MIXER_B.8, MIXER_B.12
- net 2164_OUT4_MIXA: now also 2164A.13, I_SUM.6; no longer JP_MIXER_A.8, MIXER_A.13
- net 2164_OUT4_MIXB: now also 2164B.13, I_SUM.12; no longer JP_MIXER_B.6, MIXER_B.13
- net 3V3: now also 24C04.2, 24C04.3, 24C04.8, C65.+, C66.2, C67.2, C68.2, C69.2, C70.2, C71.2, F446.1, F446.13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; no longer C_DEC_1.2, C_DEC_2.2, C_DEC_3.2, C_DEC_4.2, C_DEC_5.2, C_DEC_6.2, C_TLV_OUT.+, DEBUG_CONN.1, I2C_PU_SCL.2, I2C_PU_SDA.2, IC2.2, IC2.3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
- net 5V: now also 0V/5V/-15V/+15V.3, 0V/5V/-15V/+15V.4, AD5644.9, ADG453.12, BH2221.10, BH2221.11, C51.1, C58.+, C59.+, C61.2, C62.+, C72.2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; no longer 3.12, C5V_VCF.1, CDEC_411B6.1, CDEC_411B7.1, CONN_ALIM.3, CONN_ALIM.4, C_DEC_ALIM_5V.+, C_IN_ALIM_POL.+, IC1.12, REG3V3.1, REG3V3.3, R_PD_411_IN_SAW1.2
- net BIAS_VCA: now also C37.1, R50.2, R51.2, R52.1, SUM_OPAMP.3, VCA.4; no longer C1_VCA.1, C2_VCA.1, R3_VCA.1, R4_VCA.2, R5_VCA.1, VCA.3
- net BOOT1: now also F446.60, R81.1; no longer R_BOOT1.1, U1.60
- net CALIB_3340A: now also CAL_A.P$1, R6.1, R8.1; no longer R5_3.1, R6_3.1, U1.14
- net CALIB_3340B: now also CAL_B.P$1, R5.1, R7.1; no longer R5_1.1, R6_1.1, U1.15
- net CAP1_VCF: now also C43.2, VCF1.5; no longer C3.2, VCF.5
- net CAP2_VCF: now also C45.2, VCF1.4; no longer C5.2, VCF.4
- net CAP3_VCF: now also C49.2, VCF1.16; no longer C4.2, VCF.16
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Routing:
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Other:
- board size 163.3 x 134.6 mm -> 101.1 x 99.1 mm
- board text removed: "VCO3340B"

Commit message: PCB update
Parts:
- added +15V, -15V, GREEN: (no value), Passives:0805-LED
- added 5V, RED1, RED2: (no value), Passives:0603-LED
- added I2C, MIDI: (no value), con-lstb:MA03-1
- added R89, R90, R91, R92, R93, R94: 330, MyComponents:R0805
- moved C72 4.21 mm to (40.3, 57.5)
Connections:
- new net LED1_PWM: F446.22, R90.1
- new net LED2_PWM: F446.38, R89.1
- new net LED3_PWM: F446.26, R91.1
- new net N$48: R89.2, RED1.A
- new net N$52: R91.2, RED2.A
- new net N$53: 5V.A, R92.2
- new net N$54: -15V.A, R93.2
- new net N$55: +15V.A, R94.2
- new net N$56: GREEN.A, R90.2
- new net USART1_RX: F446.59, MIDI.1
- new net USART1_TX: F446.58, MIDI.2
- net +15V: now also R94.1
- net -15V: now also R93.1
- net 5V: now also R92.1
- net GND: now also +15V.C, -15V.C, 5V.C, GREEN.C, I2C.3, MIDI.3, RED1.C, RED2.C
- net SCL: now also I2C.2
- net SDA: now also I2C.1
- net SW1: now also F446.40
- net SW2: now also F446.39
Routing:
- net GND: track 941.8 -> 988.2 mm
- net SW1: track 2.79 -> 38.7 mm, vias 0 -> 2
- net USART1_RX: track 0.00 -> 27.6 mm, vias 0 -> 1
- net SW2: track 2.79 -> 28.2 mm, vias 0 -> 2
- net USART1_TX: track 0.00 -> 22.9 mm, vias 0 -> 1
- net LED1_PWM: track 0.00 -> 16.0 mm, vias 0 -> 2
- net SDA: track 24.0 -> 35.4 mm
- net LED3_PWM: track 0.00 -> 9.40 mm, vias 0 -> 2
- net SCL: track 26.8 -> 35.5 mm
- net -15V: track 359.2 -> 363.0 mm
- net N$56: track 0.00 -> 3.64 mm
- net N$53: track 0.00 -> 3.33 mm
- net N$55: track 0.00 -> 3.24 mm
- net N$54: track 0.00 -> 3.24 mm
- net LED2_PWM: track 0.00 -> 2.76 mm
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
